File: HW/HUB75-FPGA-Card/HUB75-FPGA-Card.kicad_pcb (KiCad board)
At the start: 4 copper layers, 53.3 x 85.1 mm, 117 parts, among them J1 Conn_02x04_Odd_Even, J10 USB_A_Stacked, J11 Conn_01x01, J12 Conn_01x01, J13 Conn_01x01, J14 Conn_01x01, J15 Conn_01x01, J16 Conn_01x01, J2 Conn_01x03, J3 Conn_02x08_Odd_Even, J4 Conn_01x03, J5 Conn_01x03, J6 Conn_02x08_Odd_Even, J7 Conn_01x03, J8 Conn_01x04, J9 USB_C_Receptacle_USB2.0, U1 T20Q100F3, U10 HS-100B, U11 PAM8406, U12 USBLC6-2SC6, U13 CH334R, U2 XC6206PxxxMR, U3 AP2112K-1.2, U4 74AHCT245PW, U5 74AHCT245PW, U6 74AHCT245PW, U7 FT232H, U8 93LCxxBxxOT, U9 WMM7037AT2, X1 ECS-2520MV-xxx-xx, Y1 Crystal_GND24

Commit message: saving hardware progress
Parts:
- removed C42, C43: 10u, Capacitor_SMD:C_0603_1608Metric
- removed C44, C45: 100n, Capacitor_SMD:C_0603_1608Metric
- removed C50: 1u, Capacitor_SMD:C_0603_1608Metric
- removed J10: USB_A_Stacked, Connector_USB:USB_A_CUI_UJ2-ADH-TH_Horizontal_Stacked
- removed J13, J14, J15, J16: Conn_01x01, Connector_Wire:SolderWirePad_1x01_SMD_1x2mm
- added U14: RP2040, Package_DFN_QFN:QFN-56-1EP_7x7mm_P0.4mm_EP3.2x3.2mm, F.Cu at (154.0, 111.7)
- J8: value Conn_01x04 -> USB_A; footprint TerminalBlock_Phoenix:TerminalBlock_Phoenix_PT-1,5-4-5.0-H_1x04_P5.00mm_Horizontal -> Project:SS-52100-002
- J9: value USB_C_Receptacle_USB2.0 -> USB_C_Receptacle_USB2.0_14P; footprint Connector_USB:USB_C_Receptacle_GCT_USB4105-xx-A_16P_TopMnt_Horizontal -> Project:GCT_USB4145-03-0170-C_REVA2
- U11: value PAM8406 -> W25Q128JVS; footprint Package_SO:SO-16_3.9x9.9mm_P1.27mm -> Package_SO:SOIC-8_5.23x5.23mm_P1.27mm
- moved U11 47.2 mm to (154.5, 103.7), turned to 0 degrees
- moved C48 43.9 mm to (77.6, 117.9)
- moved C49 42.4 mm to (76.1, 117.9), turned to -90 degrees
- moved D1 41.2 mm to (66.3, 112.8)
- moved R18 41.2 mm to (66.9, 110.0)
- moved R19 41.2 mm to (66.9, 106.9)
- moved U10 41.2 mm to (72.9, 108.7)
- moved C36 41.2 mm to (77.6, 103.9)
- moved C37 41.2 mm to (79.9, 105.4)
- moved C38 41.2 mm to (79.9, 106.9)
- moved C39 41.2 mm to (79.9, 113.0)
- moved C40 41.2 mm to (79.9, 110.0)
- moved C41 41.2 mm to (79.9, 111.5)
- moved FB4 41.2 mm to (79.9, 103.9)
- moved FB5 41.2 mm to (79.9, 108.5)
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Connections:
- C48 pad 2: Net-(U11-INL) -> unconnected-(C48-Pad2)
- C49 pad 2: Net-(U11-INR) -> unconnected-(C49-Pad2)
- J1 pad 7: GND -> /FPGA/SS
- J8 pad 1: /USB Audio/L+ -> +5V
- J8 pad 2: /USB Audio/L- -> /USB Hub/USB_EXT_D-
- J8 pad 3: /USB Audio/R- -> /USB Hub/USB_EXT_D+
- J8 pad 4: /USB Audio/R+ -> GND
- J9 pad A8: unconnected-(J9-SBU1-PadA8) -> (no net)
- J9 pad B8: unconnected-(J9-SBU2-PadB8) -> (no net)
- R1 pad 2: Net-(U1B-GPIOL_00_SS_N) -> /FPGA/SS
- U1 pad 24: Net-(U1B-GPIOL_00_SS_N) -> /FPGA/SS
- U1 pad 6: Net-(U1B-GPIOL_00_SS_N) -> /FPGA/SS
- U11 pad 1: /USB Audio/L+ -> unconnected-(U11-~{CS}-Pad1)
- U11 pad 2: GND -> unconnected-(U11-DO(IO1)-Pad2)
- U11 pad 3: /USB Audio/L- -> unconnected-(U11-IO2-Pad3)
- U11 pad 4: +5V -> unconnected-(U11-GND-Pad4)
- U11 pad 5: +5V -> unconnected-(U11-DI(IO0)-Pad5)
- U11 pad 6: +5V -> unconnected-(U11-CLK-Pad6)
- U11 pad 7: Net-(U11-INL) -> unconnected-(U11-IO3-Pad7)
- U11 pad 8: Net-(U11-VREF) -> unconnected-(U11-VCC-Pad8)
- U12 pad 1: /USB Hub/USBU_D+ -> /USB Hub/USBU_D-
- U12 pad 3: /USB Hub/USBU_D- -> /USB Hub/USBU_D+
- U12 pad 4: /USB Hub/RAW_D- -> /USB Hub/RAW_D+
- U12 pad 6: /USB Hub/RAW_D+ -> /USB Hub/RAW_D-
- U13 pad 3: /USB Hub/USB4_D- -> /USB Audio/USB_D-
- U13 pad 4: /USB Hub/USB4_D+ -> /USB Audio/USB_D+
- U13 pad 5: /USB Hub/USB3_D- -> /MCU/USB_D-
- U13 pad 6: /USB Hub/USB3_D+ -> /MCU/USB_D+
- U13 pad 7: /USB Audio/USB_D- -> /USB Hub/USB_EXT_D-
- U13 pad 8: /USB Audio/USB_D+ -> /USB Hub/USB_EXT_D+
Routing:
- net +5V: track 93.7 -> 45.1 mm, vias 22 -> 24
- net /FPGA/SS: track 0.00 -> 47.6 mm, vias 0 -> 2
- net /USB Audio/R+: track 33.7 -> 0.00 mm, vias 1 -> 0
- net /USB Hub/USB4_D+: track 31.4 -> 0.00 mm
- net /USB Hub/USB4_D-: track 31.0 -> 0.00 mm
- net /USB Hub/USB3_D+: track 30.3 -> 0.00 mm
- net /USB Audio/L+: track 29.7 -> 0.00 mm, vias 1 -> 0
- net /USB Hub/USB3_D-: track 29.7 -> 0.00 mm
- net /USB Audio/R-: track 28.9 -> 0.00 mm, vias 1 -> 0
- net GND: track 231.0 -> 203.0 mm, vias 48 -> 46
- net /USB Audio/L-: track 27.6 -> 0.00 mm, vias 1 -> 0
- net Net-(U1B-GPIOL_00_SS_N): track 20.4 -> 0.00 mm, vias 2 -> 0
- net /USB Audio/USB_D+: track 17.2 -> 0.00 mm
- net /USB Audio/USB_D-: track 17.1 -> 0.00 mm
- net /USB Hub/USB_EXT_D-: track 0.00 -> 15.1 mm
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- removed copper zone on F.Cu, net /USB Audio/L+
- removed copper zone on F.Cu, net /USB Audio/L-
- removed copper zone on F.Cu, net /USB Audio/R+
- removed copper zone on F.Cu, net /USB Audio/R-
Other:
- board text added: "3V3 TDO TDI TCK RST TMS GND SS"
- board text removed: "+L-"
- board text removed: "-R+"
- board text removed: "3V3 TDO TDI TCK RST TMS GND GND"
- board text removed: "Aux 5V"

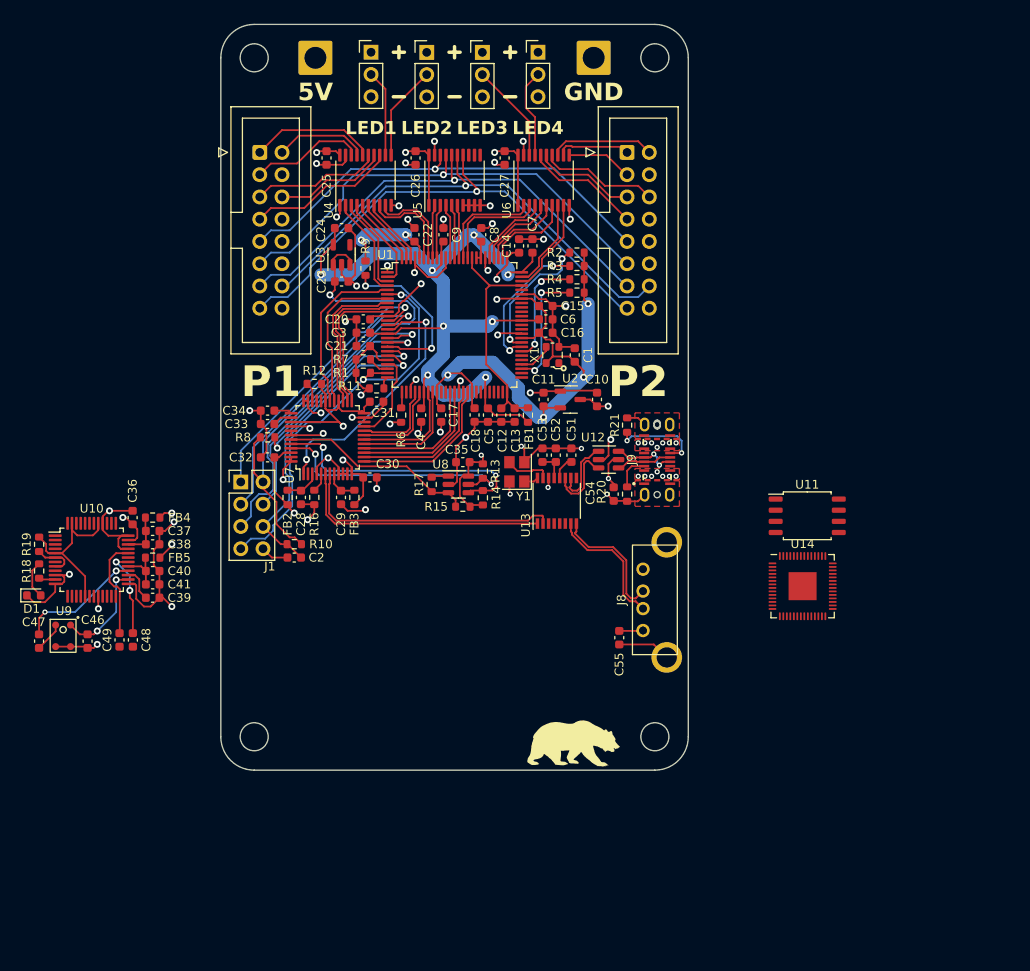
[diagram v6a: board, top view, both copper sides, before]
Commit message: initial v1.1 board layout
still needs rp2040 pins routed
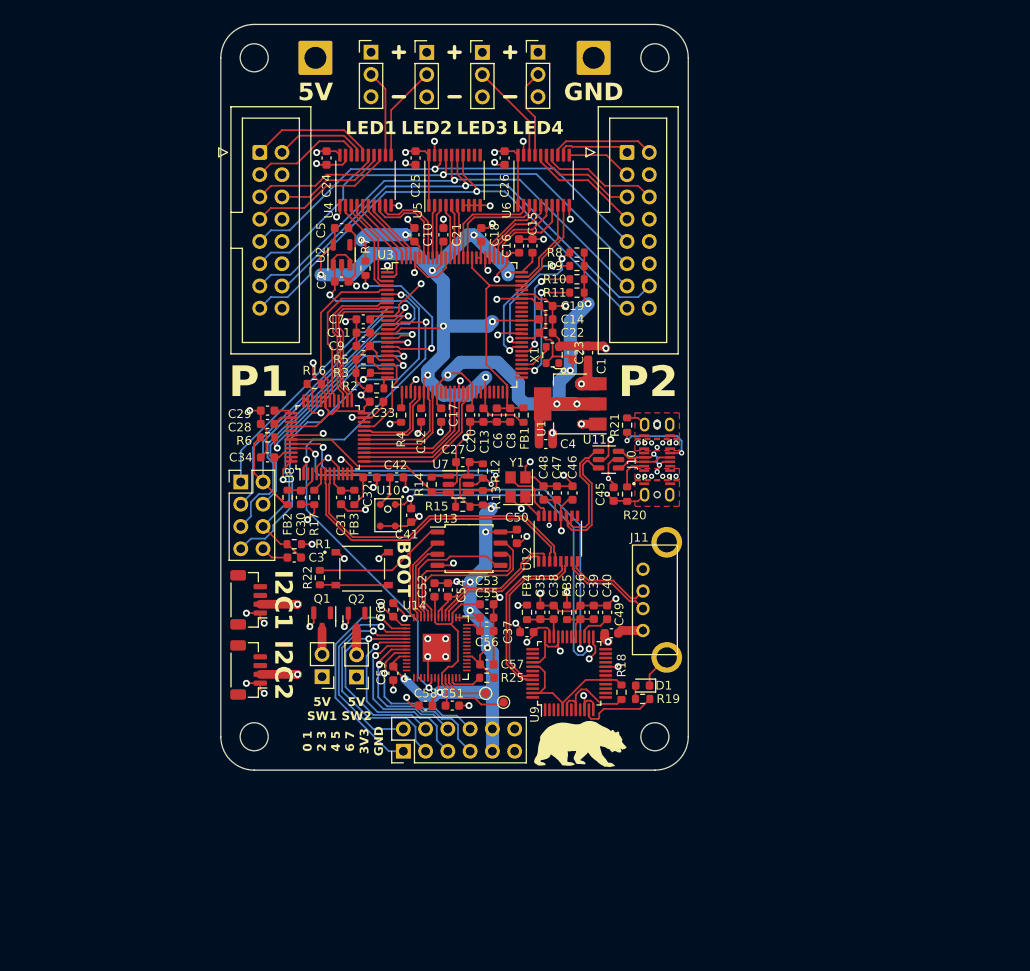
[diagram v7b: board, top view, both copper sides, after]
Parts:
- removed the C48 at (77.6, 117.9)
- removed the C49 at (76.1, 117.9)
- removed the U2 at (127.5, 90.4)
- added C50: 100n, Capacitor_SMD:C_0603_1608Metric, F.Cu at (121.4, 106.0)
- added C51: 100n, Capacitor_SMD:C_0603_1608Metric, F.Cu at (114.0, 125.3)
- added C52: 100n, Capacitor_SMD:C_0603_1608Metric, F.Cu at (112.0, 112.2)
- added C53: 1u, Capacitor_SMD:C_0603_1608Metric, F.Cu at (118.0, 113.8)
- added C54: 1u, Capacitor_SMD:C_0603_1608Metric, F.Cu at (113.5, 112.2)
- added C55: 100n, Capacitor_SMD:C_0603_1608Metric, F.Cu at (118.0, 115.3)
- added C56: 100n, Capacitor_SMD:C_0603_1608Metric, F.Cu at (118.0, 116.8)
- added C57: 100n, Capacitor_SMD:C_0603_1608Metric, F.Cu at (118.0, 120.7)
- added C58: 100n, Capacitor_SMD:C_0603_1608Metric, F.Cu at (111.0, 125.3)
- added C59: 100n, Capacitor_SMD:C_0603_1608Metric, F.Cu at (107.3, 121.7)
- added C60: 100n, Capacitor_SMD:C_0603_1608Metric, F.Cu at (107.3, 114.4)
- added J12: Conn_02x06_Odd_Even, Connector_PinHeader_2.54mm:PinHeader_2x06_P2.54mm_Vertical, F.Cu at (108.5, 130.6)
- added J13: Conn_01x02, Connector_PinHeader_2.54mm:PinHeader_1x02_P2.54mm_Vertical, F.Cu at (99.2, 122.1)
- added J14: Conn_01x02, Connector_PinHeader_2.54mm:PinHeader_1x02_P2.54mm_Vertical, F.Cu at (103.1, 122.1)
- added J16: Conn_01x04, Connector_JST:JST_SH_BM04B-SRSS-TB_1x04-1MP_P1.00mm_Vertical, F.Cu at (90.8, 113.3)
- added J17: Conn_01x04, Connector_JST:JST_SH_BM04B-SRSS-TB_1x04-1MP_P1.00mm_Vertical, F.Cu at (90.8, 121.3)
- added Q1: AO3400A, Package_TO_SOT_SMD:SOT-23, F.Cu at (99.2, 115.7)
- added Q2: AO3400A, Package_TO_SOT_SMD:SOT-23, F.Cu at (103.1, 115.7)
- added R22: 2.2k, Resistor_SMD:R_0603_1608Metric, F.Cu at (98.9, 110.7)
- added R25: 10k, Resistor_SMD:R_0603_1608Metric, F.Cu at (118.0, 122.2)
- added SW1: SW_Push, Project:SW_TS-1187A-B-A-B, F.Cu at (103.8, 109.7)
- added TP1: TestPoint, TestPoint:TestPoint_Pad_D1.0mm, F.Cu at (119.9, 125.0)
- added TP2: TestPoint, TestPoint:TestPoint_Pad_D1.0mm, F.Cu at (117.9, 124.0)
- added U1: AMS1117-3.3, Package_TO_SOT_SMD:SOT-223-3_TabPin2, F.Cu at (127.5, 90.9)
- C4: renamed from C11; value 1u -> 10u
- moved R19 70.4 mm to (135.8, 124.6), turned to 180 degrees
- moved D1 70.2 mm to (135.8, 123.1), turned to 180 degrees
- moved R18 68.6 mm to (133.3, 123.8)
- moved U9 56.0 mm to (127.4, 121.7), turned to 90 degrees
- moved C40 51.9 mm to (131.7, 114.7), turned to 90 degrees
- moved C39 50.4 mm to (130.2, 114.7), turned to 90 degrees
- moved C36 49.0 mm to (128.7, 114.7), turned to 90 degrees
- moved FB5 47.7 mm to (127.1, 114.7), turned to -90 degrees
- moved C37 46.8 mm to (122.6, 117.0), turned to 180 degrees
- moved C38 46.4 mm to (125.6, 114.7), turned to 90 degrees
- moved C35 45.2 mm to (124.1, 114.7), turned to 90 degrees
- moved C42 44.9 mm to (107.7, 99.3), turned to 180 degrees
- moved FB4 44.1 mm to (122.6, 114.7), turned to -90 degrees
- moved U14 42.3 mm to (112.3, 118.7)
- moved C41 39.6 mm to (109.3, 103.6)
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- renumbered C10 to C1, C22 to C10, C3 to C11, C4 to C12, C5 to C13, C6 to C14, C7 to C15, C14 to C16, C8 to C18, C15 to C19, C23 to C2, C18 to C20, C9 to C21, C16 to C22, C1 to C23, C25 to C24, C26 to C25, C27 to C26, C35 to C27, C33 to C28, C34 to C29, C2 to C3, C28 to C30, C29 to C31, C30 to C32, C31 to C33, C32 to C34, C37 to C35, C40 to C36, C36 to C37, C41 to C39, C39 to C40, C46 to C41, C47 to C42, C54 to C45, C51 to C46, C52 to C47, C53 to C48, C55 to C49, C24 to C5, C12 to C6, C20 to C7, C13 to C8, C21 to C9, H3 to H2, H2 to H3, J9 to J10, J8 to J11, J3 to J2, J6 to J3, J11 to J4, J12 to J5, J2 to J6, J4 to J7, J5 to J8, J7 to J9, R10 to R1, R4 to R10, R5 to R11, R13 to R12, R14 to R13, R17 to R14, R12 to R16, R16 to R17, R19 to R18, R18 to R19, R11 to R2, R1 to R3, R6 to R4, R7 to R5, R8 to R6, R9 to R7, R2 to R8, R3 to R9, U9 to U10, U12 to U11, U13 to U12, U11 to U13, U3 to U2, U1 to U3, U8 to U7, U7 to U8, U10 to U9
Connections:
- C27 pad 1: +3.3VP -> +3V3
- C32 pad 1: +3.3VP -> +3V3
- C33 pad 1: +3.3VP -> +3V3
- C34 pad 1: +3.3VP -> +3V3
- FB2 pad 1: +3.3VP -> +3V3
- FB3 pad 1: +3.3VP -> +3V3
- R12 pad 1: +3.3VP -> +3V3
- R13 pad 1: +3.3VP -> +3V3
- R15 pad 1: +3.3VP -> +3V3
- R16 pad 2: +3.3VP -> +3V3
- U12 pad 1: /FTDI/USB_D- -> /MCU/USB_D-
- U12 pad 2: /FTDI/USB_D+ -> /MCU/USB_D+
- U12 pad 3: /USB Audio/USB_D- -> /FTDI/USB_D-
- U12 pad 4: /USB Audio/USB_D+ -> /FTDI/USB_D+
- U12 pad 5: /MCU/USB_D- -> /USB Audio/USB_D-
- U12 pad 6: /MCU/USB_D+ -> /USB Audio/USB_D+
- U13 pad 1: unconnected-(U11-~{CS}-Pad1) -> Net-(U13-~{CS})
- U13 pad 2: unconnected-(U11-DO(IO1)-Pad2) -> Net-(U13-DO(IO1))
- U13 pad 3: unconnected-(U11-IO2-Pad3) -> Net-(U13-IO2)
- U13 pad 4: unconnected-(U11-GND-Pad4) -> GND
- U13 pad 5: unconnected-(U11-DI(IO0)-Pad5) -> Net-(U13-DI(IO0))
- U13 pad 6: unconnected-(U11-CLK-Pad6) -> Net-(U13-CLK)
- U13 pad 7: unconnected-(U11-IO3-Pad7) -> Net-(U13-IO3)
- U13 pad 8: unconnected-(U11-VCC-Pad8) -> +3V3
- U14 pad 1: Net-(U14-IOVDD-Pad1) -> +3V3
- U14 pad 10: Net-(U14-IOVDD-Pad1) -> +3V3
- U14 pad 19: unconnected-(U14-TESTEN-Pad19) -> GND
- U14 pad 2: unconnected-(U14-GPIO0-Pad2) -> /MCU/GPIO0
- U14 pad 20: unconnected-(U14-XIN-Pad20) -> /FPGA/CLK_12MHZ
- U14 pad 22: Net-(U14-IOVDD-Pad1) -> +3V3
- U14 pad 23: Net-(U14-DVDD-Pad23) -> +1V1
- U14 pad 24: unconnected-(U14-SWCLK-Pad24) -> Net-(U14-SWCLK)
- U14 pad 25: unconnected-(U14-SWD-Pad25) -> Net-(U14-SWD)
- U14 pad 26: unconnected-(U14-RUN-Pad26) -> Net-(U14-RUN)
- U14 pad 3: unconnected-(U14-GPIO1-Pad3) -> /MCU/GPIO1
- U14 pad 33: Net-(U14-IOVDD-Pad1) -> +3V3
- U14 pad 4: unconnected-(U14-GPIO2-Pad4) -> /MCU/GPIO2
- U14 pad 42: Net-(U14-IOVDD-Pad1) -> +3V3
- U14 pad 43: unconnected-(U14-ADC_AVDD-Pad43) -> +3V3
- U14 pad 44: unconnected-(U14-VREG_IN-Pad44) -> +3V3
- U14 pad 45: unconnected-(U14-VREG_VOUT-Pad45) -> +1V1
- U14 pad 46: unconnected-(U14-USB_DM-Pad46) -> /MCU/USB_D-
- U14 pad 47: unconnected-(U14-USB_DP-Pad47) -> /MCU/USB_D+
- U14 pad 48: unconnected-(U14-USB_VDD-Pad48) -> +3V3
- U14 pad 49: Net-(U14-IOVDD-Pad1) -> +3V3
- U14 pad 5: unconnected-(U14-GPIO3-Pad5) -> /MCU/GPIO3
- U14 pad 50: Net-(U14-DVDD-Pad23) -> +1V1
- U14 pad 51: unconnected-(U14-QSPI_SD3-Pad51) -> Net-(U13-IO3)
- U14 pad 52: unconnected-(U14-QSPI_SCLK-Pad52) -> Net-(U13-CLK)
- U14 pad 53: unconnected-(U14-QSPI_SD0-Pad53) -> Net-(U13-DI(IO0))
- U14 pad 54: unconnected-(U14-QSPI_SD2-Pad54) -> Net-(U13-IO2)
- U14 pad 55: unconnected-(U14-QSPI_SD1-Pad55) -> Net-(U13-DO(IO1))
- U14 pad 56: unconnected-(U14-QSPI_SS-Pad56) -> Net-(U13-~{CS})
- U14 pad 57: unconnected-(U14-GND-Pad57) -> GND
- U14 pad 6: unconnected-(U14-GPIO4-Pad6) -> /MCU/GPIO4
- U14 pad 7: unconnected-(U14-GPIO5-Pad7) -> /MCU/GPIO5
- U14 pad 8: unconnected-(U14-GPIO6-Pad8) -> /MCU/GPIO6
- U14 pad 9: unconnected-(U14-GPIO7-Pad9) -> /MCU/GPIO7
- U7 pad 6: +3.3VP -> +3V3
- U8 pad 12: +3.3VP -> +3V3
- U8 pad 24: +3.3VP -> +3V3
- U8 pad 28: +3.3VP -> +3V3
- U8 pad 31: +3.3VP -> +3V3
- U8 pad 39: +3.3VP -> +3V3
- U8 pad 40: +5V -> +3V3
- U8 pad 46: +3.3VP -> +3V3
- U9 pad 30: Net-(U10-LOL) -> unconnected-(U9-LOL-Pad30)
- U9 pad 32: Net-(U10-LOR) -> unconnected-(U9-LOR-Pad32)
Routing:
- net +3V3: track 212.7 -> 414.4 mm, vias 12 -> 26
- net +3.3VP: track 75.4 -> 0.00 mm, vias 4 -> 0
- net /FPGA/CLK_12MHZ: track 30.0 -> 63.0 mm, vias 2 -> 3
- net Net-(U10-VDD): track 11.8 -> 41.2 mm
- net /MCU/GPIO2: track 0.00 -> 26.6 mm, vias 0 -> 1
- net /MCU/GPIO0: track 0.00 -> 26.3 mm, vias 0 -> 1
- net GND: track 203.0 -> 227.4 mm, vias 46 -> 71
- net Net-(U9-MICIN): track 14.3 -> 38.6 mm
- net /MCU/GPIO1: track 0.00 -> 23.6 mm, vias 0 -> 1
- net /MCU/GPIO4: track 0.00 -> 23.0 mm, vias 0 -> 1
- net Net-(U13-~{CS}): track 0.00 -> 22.9 mm
- net /MCU/GPIO3: track 0.00 -> 22.8 mm, vias 0 -> 1
- net /MCU/GPIO6: track 0.00 -> 21.8 mm, vias 0 -> 1
- net +1V1: track 0.00 -> 20.7 mm
- net /USB Audio/USB_D-: track 0.00 -> 20.3 mm
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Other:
- board text added: "0 1 2 3 4 5 6 7"
- board text added: "3V3"
- board text added: "5V SW1"
- board text added: "5V SW2"
- board text added: "BOOT"
- board text added: "I2C1"
- board text added: "I2C2"
- board text added: "Prototypical V1.1"
- board text removed: "Prototypical Helmet Controller V1.1"

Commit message: finish rp2040 routing
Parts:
- moved C59 1.49 mm to (105.9, 122.2)
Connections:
- J12 pad 7: /MCU/GPIO6 -> /MCU/GPIO26
- J12 pad 8: /MCU/GPIO7 -> /MCU/GPIO27
- U14 pad 11: unconnected-(U14-GPIO8-Pad11) -> /MCU/SDA0
- U14 pad 12: unconnected-(U14-GPIO9-Pad12) -> /MCU/SCL0
- U14 pad 17: unconnected-(U14-GPIO14-Pad17) -> /MCU/SDA1
- U14 pad 18: unconnected-(U14-GPIO15-Pad18) -> /MCU/SCL1
- U14 pad 38: unconnected-(U14-GPIO26_ADC0-Pad38) -> /MCU/GPIO26
- U14 pad 39: unconnected-(U14-GPIO27_ADC1-Pad39) -> /MCU/GPIO27
- U14 pad 8: /MCU/GPIO6 -> /MCU/5VSW_1
- U14 pad 9: /MCU/GPIO7 -> /MCU/5VSW_2
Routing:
- net +3V3: track 414.4 -> 189.9 mm
- net /MCU/SDA0: track 0.00 -> 32.8 mm
- net /MCU/SCL0: track 0.00 -> 29.3 mm
- net /MCU/SCL1: track 0.00 -> 24.3 mm, vias 0 -> 2
- net /MCU/GPIO6: track 21.8 -> 0.00 mm, vias 1 -> 0
- net /MCU/SDA1: track 0.00 -> 21.1 mm
- net /MCU/5VSW_1: track 0.00 -> 18.2 mm, vias 0 -> 2
- net /MCU/GPIO7: track 18.1 -> 0.00 mm, vias 1 -> 0
- net /MCU/GPIO26: track 0.00 -> 15.0 mm, vias 0 -> 1
- net /MCU/5VSW_2: track 0.00 -> 14.6 mm, vias 0 -> 2
- net /MCU/GPIO27: track 0.00 -> 13.8 mm, vias 0 -> 1
- net GND: track 227.4 -> 226.0 mm
- net /MCU/GPIO4: track 23.0 -> 22.1 mm
- net Net-(U3B-GPIOL_09_CDI1): track 19.1 -> 19.7 mm
- net +5V: track 44.7 -> 44.2 mm
- added copper zone on In2.Cu, net +3V3
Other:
- board text added: "0 1 2 3 4 5 26 27"
- board text added: "[3V3]"
- board text added: "[GND]"
- board text removed: "0 1 2 3 4 5 6 7"
- board text removed: "3V3"
